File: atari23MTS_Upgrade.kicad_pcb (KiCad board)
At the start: 2 copper layers, 164.5 x 93 mm, 83 parts, among them J1 Micro_SD_Card_Det, P1 CONN_01X01, P2 CONN_01X01, P3 CONN_01X01, P4 CONN_01X01, P5 CONN_01X01, P6 CONN_01X01, SW1 SW_PUSH, U1 NCP1117ST33T3G, U10 ISSI61WV5128BL, U11 ISSI61WV5128BL, U12 ISSI61WV5128BL, U13 ISSI61WV5128BL, U14 74LS08, U15 74LS08, U16 74LS08, U17 STM32F407VETx, U2 74LS138, U3 74HC04, U4 TXB0108-PW, U5 TXB0108-PW, U6 TXB0108-PW, U7 74HC04, U8 TXB0108-PW, U9 TXB0108-PW

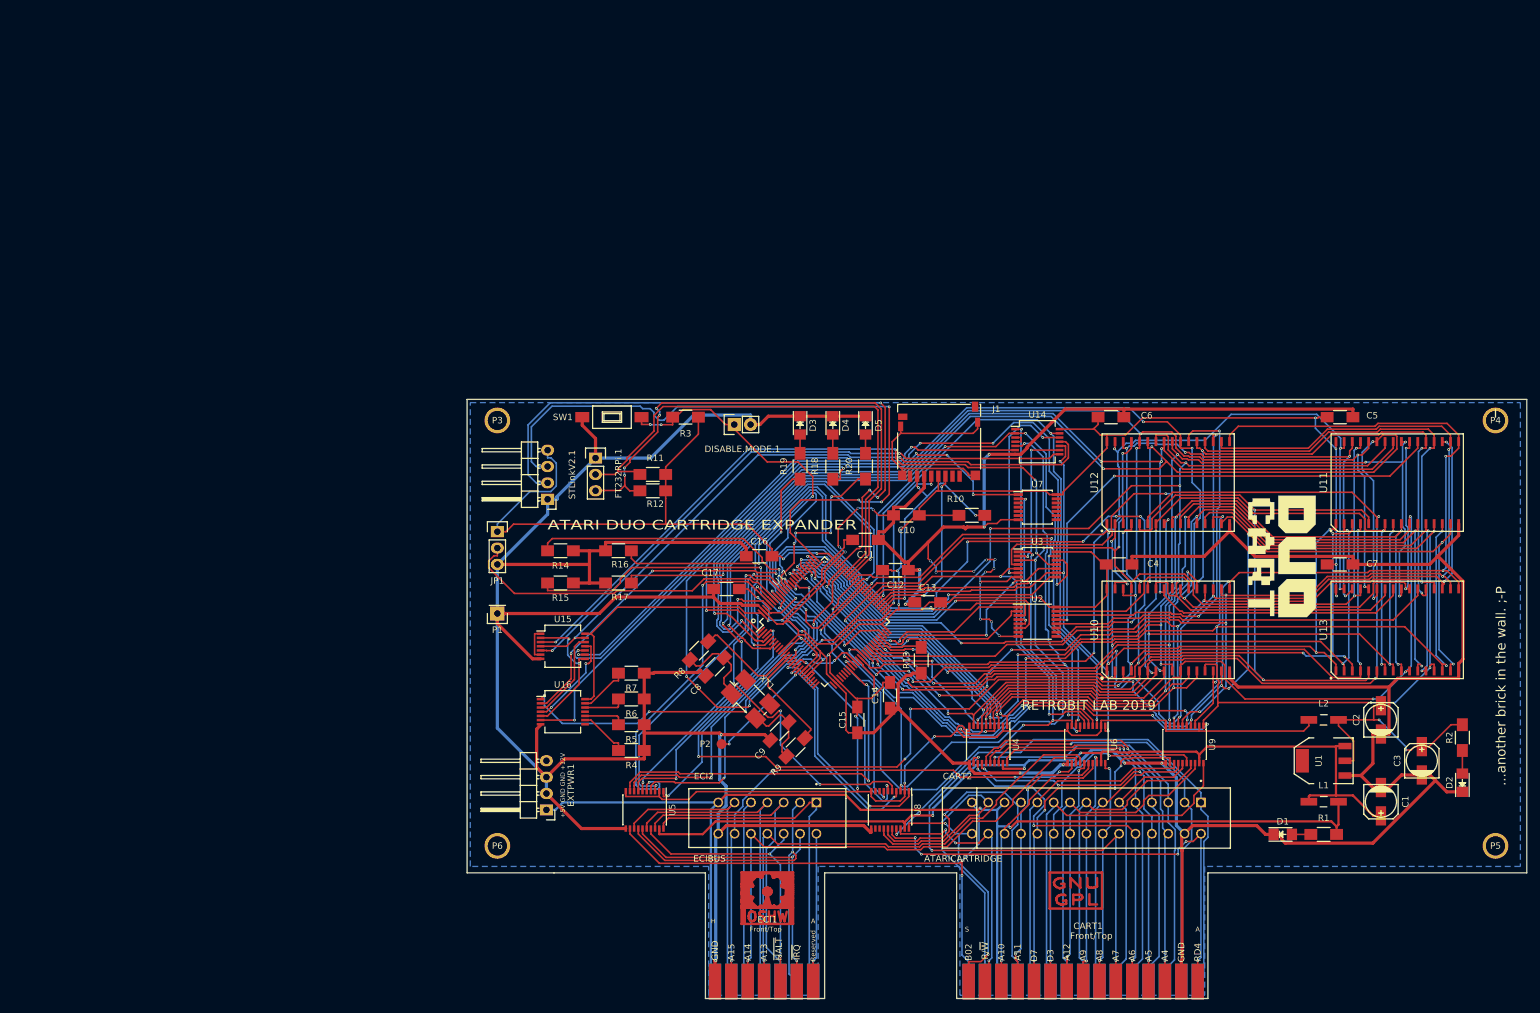
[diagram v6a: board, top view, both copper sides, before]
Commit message: Upgraded with the latest infos
Now there is no logic for address/decoding. All is done inside the
microprocessor. This is a semi-final release.
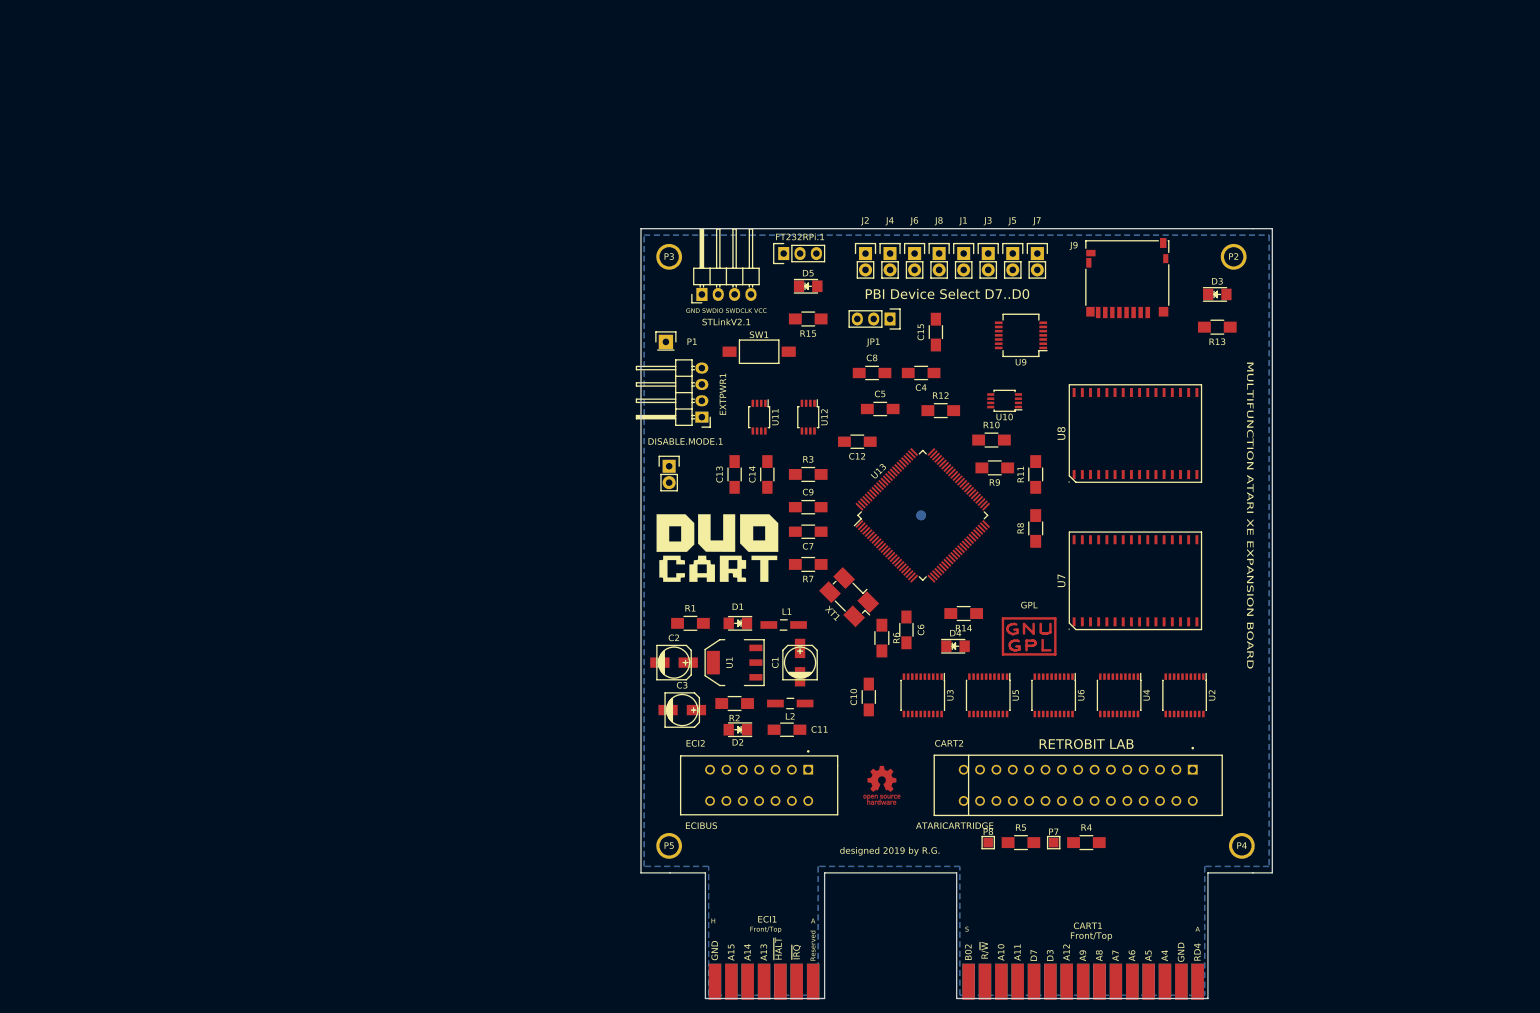
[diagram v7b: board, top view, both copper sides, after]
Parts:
- removed ATARI LOGO FUJI: LOGO, RetroBitLab:atari_fuji_SilkScreen_21.2x25-RevBack
- removed C16, C17: 100n, Capacitors_SMD:C_1206_HandSoldering
- removed R16, R17: 0, Resistors_SMD:R_1206_HandSoldering
- removed R18, R19, R20: 220, Resistors_SMD:R_1206_HandSoldering
- removed REF**: Symbol_GNU-GPL_CopperTop_Small, Symbol:Symbol_GNU-GPL_CopperTop_Small
- removed REF**: Symbol_OSHW-Logo_CopperTop_Negative, Symbols:Symbol_OSHW-Logo_CopperTop_Negative
- removed U14, U15, U16: 74LS08, Housings_SSOP:SSOP-14_5.3x6.2mm_Pitch0.65mm
- removed U17: STM32F407VETx, Housings_QFP:LQFP-100_14x14mm_Pitch0.5mm
- added ATARILOGO: LOGO, RetroBitLab:atari_fuji_SilkScreen_21.2x25-RevBack, B.Cu at (142.2, 49.5)
- added G***: LOGO, RetroBitLab:atari_800_XL_BW_25x25, B.Cu at (144.8, 74.9)
- added GPL: Symbol_GNU-GPL_CopperTop_Small, Symbol:Symbol_GNU-GPL_CopperTop_Small, F.Cu at (158.8, 82.5)
- added J2: Conn_01x02, Pin_Headers:Pin_Header_Straight_1x02, F.Cu at (133.3, 22.9)
- added J3: Conn_01x02, Pin_Headers:Pin_Header_Straight_1x02, F.Cu at (152.4, 22.9)
- added J4: Conn_01x02, Pin_Headers:Pin_Header_Straight_1x02, F.Cu at (137.2, 22.9)
- added J5: Conn_01x02, Pin_Headers:Pin_Header_Straight_1x02, F.Cu at (156.2, 22.9)
- added J6: Conn_01x02, Pin_Headers:Pin_Header_Straight_1x02, F.Cu at (141.0, 22.9)
- added J7: Conn_01x02, Pin_Headers:Pin_Header_Straight_1x02, F.Cu at (160.0, 22.9)
- added J8: Conn_01x02, Pin_Headers:Pin_Header_Straight_1x02, F.Cu at (144.8, 22.9)
- added J9: Micro_SD_Card_Det, RetroBitLab:microSD_HC_Hirose_DM3D-SF, F.Cu at (174.0, 26.7)
- added OSHW: OSHW-Logo_5.7x6mm_Copper, Symbol:OSHW-Logo_5.7x6mm_Copper, F.Cu at (135.9, 105.4)
- added P7: CONN_01X01, TestPoint:TestPoint_Pad_1.5x1.5mm, F.Cu at (162.6, 114.3)
- added P8: CONN_01X01, TestPoint:TestPoint_Pad_1.5x1.5mm, F.Cu at (152.4, 114.3)
- C6, C7: value 100n -> 20p
- C8, C9: value 20p -> 100n
- J1: value Micro_SD_Card_Det -> Conn_01x02; footprint RetroBitLab:microSD_HC_Hirose_DM3D-SF -> Pin_Headers:Pin_Header_Straight_1x02
- P2: footprint Measurement_Points:Measurement_Point_Round-SMD-Pad_Small -> RetroBitLab:MountingHole
- P6: footprint RetroBitLab:MountingHole -> Measurement_Points:Measurement_Point_Round-SMD-Pad_Small; moved to B.Cu
- R10: value 47k -> 10k
- R11, R12: value 10k -> 10K
- R13, R14, R15, R7: value 0 -> 220
- R8: value 0 -> 47k
- R9: value 220 -> 10k
- SW1: value SW_PUSH -> SW_Push; footprint Buttons_Switches_SMD:SW_SPST_FSMSM -> RetroBitLab:SW_SPST_FSMSM_3D
- U10: value ISSI61WV5128BL -> 74LVC2G32; footprint RetroBitLab:SOP-32L-20.5x11.30-1.27mm -> Housings_SSOP:TSSOP-8_3x3mm_Pitch0.65mm
- U11: value ISSI61WV5128BL -> 74LVC2G08; footprint RetroBitLab:SOP-32L-20.5x11.30-1.27mm -> Housings_SSOP:TSSOP-8_3x3mm_Pitch0.65mm
- U12: value ISSI61WV5128BL -> 74LVC2G74; footprint RetroBitLab:SOP-32L-20.5x11.30-1.27mm -> Housings_SSOP:TSSOP-8_3x3mm_Pitch0.65mm
- U13: value ISSI61WV5128BL -> STM32F407VETx; footprint RetroBitLab:SOP-32L-20.5x11.30-1.27mm -> Housings_QFP:LQFP-100_14x14mm_Pitch0.5mm
- U2: value 74LS138 -> TXB0108-PW; footprint Housings_SSOP:TSSOP-16_4.4x5mm_Pitch0.65mm -> Housings_SSOP:SSOP-20_4.4x6.5mm_Pitch0.65mm
- U3: value 74HC04 -> TXB0108-PW; footprint Housings_SSOP:TSSOP-14_4.4x5mm_Pitch0.65mm -> Housings_SSOP:SSOP-20_4.4x6.5mm_Pitch0.65mm
- U7: value 74HC04 -> ISSI61WV5128BL; footprint Housings_SSOP:TSSOP-14_4.4x5mm_Pitch0.65mm -> RetroBitLab:SOP-32L-20.5x11.30-1.27mm
- U8: value TXB0108-PW -> ISSI61WV5128BL; footprint Housings_SSOP:SSOP-20_4.4x6.5mm_Pitch0.65mm -> RetroBitLab:SOP-32L-20.5x11.30-1.27mm
- U9: value TXB0108-PW -> 74HCT04; footprint Housings_SSOP:SSOP-20_4.4x6.5mm_Pitch0.65mm -> Housings_SSOP:SSOP-14_5.3x6.2mm_Pitch0.65mm
- moved P5 128.3 mm to (102.9, 114.3)
- moved C3 115.1 mm to (104.9, 93.7), turned to 0 degrees
- moved R2 113.1 mm to (113.0, 92.7), turned to 180 degrees
- moved D2 112.8 mm to (113.5, 96.8), turned to 180 degrees
- moved C2 110.1 mm to (103.6, 86.4), turned to 0 degrees
- moved P2 110.1 mm to (190.5, 22.9)
- moved R1 103.6 mm to (106.2, 80.3), turned to 0 degrees
- moved U11 99.6 mm to (116.8, 48.3), turned to 270 degrees
- moved C1 92.7 mm to (123.2, 86.4), turned to 90 degrees
- moved U1 92.7 mm to (113.0, 86.4)
- moved D1 90.7 mm to (113.5, 80.3), turned to 180 degrees
- moved L1 88.2 mm to (120.7, 80.5), turned to 180 degrees
- moved DUOCART 87.5 mm to (110.5, 68.6), turned to 0 degrees
- moved P6 83.1 mm to (142.0, 63.5)
- moved L2 82.8 mm to (121.7, 92.7), turned to 180 degrees
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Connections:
- C10 pad 1: VCC3V3 -> GND
- C10 pad 2: GND -> VCC3V3
- C6 pad 1: VCC3V3 -> Net-(C6-Pad1)
- C7 pad 1: VCC3V3 -> Net-(C7-Pad1)
- C8 pad 1: Net-(C8-Pad1) -> VCC3V3
- C9 pad 1: Net-(C9-Pad1) -> GND
- C9 pad 2: GND -> VCC3V3
- J1 pad 1: (no net) -> PBIDEV
- J1 pad 2: (no net) -> mD3
- P2 pad 1: TP1 -> (no net)
- P6 pad 1: (no net) -> TP1
- R10 pad 2: mSDO -> UART_TX_TTL
- R11 pad 2: UART_RX_TTL -> ~mCHIP0
- R12 pad 2: UART_TX_TTL -> ~mCHIP1
- R13 pad 1: GND -> Net-(D3-Pad2)
- R13 pad 2: /MCU/SPARE1 -> LEDGRN
- R14 pad 1: GND -> Net-(D4-Pad2)
- R14 pad 2: /MCU/SPARE2 -> LEDRED
- R15 pad 1: GND -> Net-(D5-Pad2)
- R15 pad 2: /MCU/SPARE3 -> LEDAMBER
- R4 pad 1: GND -> Net-(P7-Pad1)
- R4 pad 2: Net-(R4-Pad2) -> SPARE1
- R5 pad 1: GND -> Net-(P8-Pad1)
- R5 pad 2: Net-(R5-Pad2) -> SPARE2
- R6 pad 1: GND -> Net-(R6-Pad1)
- R6 pad 2: Net-(R6-Pad2) -> Net-(C6-Pad1)
- R7 pad 1: GND -> Net-(R7-Pad1)
- R7 pad 2: Net-(R7-Pad2) -> Net-(C7-Pad1)
- R8 pad 1: Net-(R8-Pad1) -> VCC3V3
- R8 pad 2: Net-(C8-Pad1) -> mSDO
- R9 pad 1: Net-(R9-Pad1) -> VCC3V3
- R9 pad 2: Net-(C9-Pad1) -> UART_RX_TTL
- U10 pad 1: mD1E2_A17 -> ~mD8XX-DFXX
- U10 pad 2: mD1E2_A16 -> Net-(U10-Pad2)
- U10 pad 3: mD1E0_A14 -> (no net)
- U10 pad 4: mD1E0_A12 -> GND
- U10 pad 5: mA7 -> (no net)
- U10 pad 6: mA6 -> (no net)
- U10 pad 7: mA5 -> ~mMPD
- U10 pad 8: mA4 -> +5VDC
- U11 pad 1: mD1E2_A17 -> mPBISEL
- U11 pad 2: mD1E2_A16 -> PBIDEV
- U11 pad 3: mD1E0_A14 -> Net-(U11-Pad3)
- U11 pad 4: mD1E0_A12 -> GND
- U11 pad 5: mA7 -> mW/~R
- U11 pad 6: mA6 -> mPBISEL
- U11 pad 7: mA5 -> Net-(U11-Pad7)
- U11 pad 8: mA4 -> +5VDC
- U12 pad 1: mD1E2_A17 -> Net-(U11-Pad3)
- U12 pad 2: mD1E2_A16 -> Net-(U11-Pad7)
- U12 pad 3: mD1E0_A14 -> Net-(U10-Pad2)
- U12 pad 4: mD1E0_A12 -> GND
- U12 pad 5: mA7 -> (no net)
- U12 pad 6: mA6 -> nRESET
- U12 pad 7: mA5 -> nRESET
- U12 pad 8: mA4 -> +5VDC
- U13 pad 1: mD1E2_A17 -> (no net)
- U13 pad 10: mA2 -> GND
- U13 pad 11: mA1 -> VCC3V3
- U13 pad 12: mA0 -> Net-(R6-Pad1)
- U13 pad 13: mD0 -> Net-(R7-Pad1)
- U13 pad 14: mD1 -> nRESET
- U13 pad 15: mD2 -> mB02/PHI2
- U13 pad 16: GND -> ~mS5
- U13 pad 17: mD3 -> ~mS4
- U13 pad 18: mD4 -> TP1
- U13 pad 19: mD5 -> VCC3V3
- U13 pad 2: mD1E2_A16 -> (no net)
- U13 pad 20: mD6 -> GND
- U13 pad 21: mD7 -> VCC3V3
- U13 pad 22: ~BSEL3 -> VCC3V3
- U13 pad 23: mD1E0_A10 -> (no net)
- U13 pad 24: ~mOE -> (no net)
- U13 pad 25: mD1E0_A11 -> (no net)
- U13 pad 26: mD1E0_A9 -> (no net)
- U13 pad 27: mD1E0_A8 -> GND
- U13 pad 28: mD1E0_A13 -> VCC3V3
- U13 pad 29: mR/~W -> (no net)
- U13 pad 3: mD1E0_A14 -> (no net)
- U13 pad 30: mD1E2_A18 -> (no net)
- U13 pad 31: mD1E0_A15 -> (no net)
- U13 pad 32: VCC3V3 -> (no net)
- U13 pad 4: mD1E0_A12 -> (no net)
- U13 pad 5: mA7 -> (no net)
- U13 pad 6: mA6 -> (no net)
- U13 pad 7: mA5 -> mPBISEL
- U13 pad 8: mA4 -> mSPARE1
- U13 pad 9: mA3 -> mSPARE2
- U2 pad 1: mD1E2_A19 -> mA0
- U2 pad 10: (no net) -> VCC3V3
- U2 pad 11: (no net) -> GND
- U2 pad 12: ~BSEL3 -> A7
- U2 pad 13: ~BSEL2 -> A6
- U2 pad 14: ~BSEL1 -> A5
- U2 pad 15: ~BSEL0 -> A4
- U2 pad 16: VCC3V3 -> A3
- U2 pad 2: mD1E3_A20 -> VCC3V3
- U2 pad 3: mD1E3_A21 -> mA1
- U2 pad 4: ~mD6XX -> mA2
- U2 pad 5: ~mD6XX -> mA3
- U2 pad 6: RAMEN -> mA4
- U2 pad 7: (no net) -> mA5
- U2 pad 8: GND -> mA6
- U2 pad 9: (no net) -> mA7
- U3 pad 1: mA10 -> ~mEXSEL
- U3 pad 10: ~mD3XX -> VCC3V3
- U3 pad 11: mD3XX -> GND
- U3 pad 12: ~mA13 -> ~CCTL
- U3 pad 13: mA13 -> ~REF
- U3 pad 14: VCC3V3 -> ~RST
- U3 pad 2: ~mA10 -> VCC3V3
- U3 pad 3: mR/~W -> ~mD1XX
- U3 pad 4: ~mOE -> ~mHALT
- U3 pad 5: mA11 -> ~mMPD
- U3 pad 6: ~mA11 -> ~mIRQ
- U3 pad 7: GND -> ~mRST
- U3 pad 8: ~mA8 -> ~mREF
- U3 pad 9: mA8 -> ~mCCTL
- U4 pad 1: mA0 -> mA8
- U4 pad 12: A7 -> A15
- U4 pad 13: A6 -> A14
- U4 pad 14: A5 -> A13
- U4 pad 15: A4 -> A12
- U4 pad 16: A3 -> A11
- U4 pad 17: A2 -> A10
- U4 pad 18: A1 -> A9
- U4 pad 20: A0 -> A8
- U4 pad 3: mA1 -> mA9
- U4 pad 4: mA2 -> mA10
- U4 pad 5: mA3 -> mA11
- U4 pad 6: mA4 -> mA12
- U4 pad 7: mA5 -> mA13
- U4 pad 8: mA6 -> mA14
- U4 pad 9: mA7 -> mA15
- U5 pad 1: ~mEXSEL -> mB02/PHI2
- U5 pad 12: ~CCTL -> SPARE2
- U5 pad 13: ~REF -> SPARE1
- U5 pad 14: ~RST -> RD5
- U5 pad 15: ~IRQ -> ~S5
- U5 pad 16: ~MPD -> RD4
- U5 pad 17: ~HALT -> ~S4
- U5 pad 18: ~D1XX -> R/~W
- U5 pad 20: ~EXSEL -> B02/PHI2
- U5 pad 3: ~mD1XX -> mR/~W
- U5 pad 4: ~mHALT -> ~mS4
- U5 pad 5: ~mMPD -> mRD4
- U5 pad 6: ~mIRQ -> ~mS5
- U5 pad 7: ~mRST -> mRD5
- U5 pad 8: ~mREF -> mSPARE1
- U5 pad 9: ~mCCTL -> mSPARE2
- U6 pad 1: mA8 -> mD0
- U6 pad 12: A15 -> D7
- U6 pad 13: A14 -> D6
- U6 pad 14: A13 -> D5
- U6 pad 15: A12 -> D4
- U6 pad 16: A11 -> D3
- U6 pad 17: A10 -> D2
- U6 pad 18: A9 -> D1
- U6 pad 20: A8 -> D0
- U6 pad 3: mA9 -> mD1
- U6 pad 4: mA10 -> mD2
- U6 pad 5: mA11 -> mD3
- U6 pad 6: mA12 -> mD4
- U6 pad 7: mA13 -> mD5
- U6 pad 8: mA14 -> mD6
- U6 pad 9: mA15 -> mD7
- U7 pad 1: mD6XX -> mxA17
- U7 pad 10: (no net) -> mA2
- U7 pad 11: (no net) -> mA1
- U7 pad 12: (no net) -> mA0
- U7 pad 13: (no net) -> mD0
- U7 pad 14: VCC3V3 -> mD1
- U7 pad 2: ~mD6XX -> mxA16
- U7 pad 3: (no net) -> mxA14
- U7 pad 4: (no net) -> mA12
- U7 pad 5: (no net) -> mA7
- U7 pad 6: (no net) -> mA6
- U7 pad 7: GND -> mA5
- U7 pad 8: (no net) -> mA4
- U7 pad 9: (no net) -> mA3
- U8 pad 1: mB02/PHI2 -> mxA17
- U8 pad 10: VCC3V3 -> mA2
- U8 pad 11: GND -> mA1
- U8 pad 12: (no net) -> mA0
- U8 pad 13: (no net) -> mD0
- U8 pad 14: RD5 -> mD1
- U8 pad 15: ~S5 -> mD2
- U8 pad 16: RD4 -> GND
- U8 pad 17: ~S4 -> mD3
- U8 pad 18: R/~W -> mD4
- U8 pad 19: VCC5V -> mD5
- U8 pad 2: VCC3V3 -> mxA16
- U8 pad 20: B02/PHI2 -> mD6
- U8 pad 3: mR/~W -> mxA14
- U8 pad 4: ~mS4 -> mA12
- U8 pad 5: mRD4 -> mA7
- U8 pad 6: ~mS5 -> mA6
- U8 pad 7: mRD5 -> mA5
- U8 pad 8: (no net) -> mA4
- U8 pad 9: (no net) -> mA3
- U9 pad 1: mD0 -> mR/~W
- U9 pad 10: VCC3V3 -> (no net)
- U9 pad 12: D7 -> (no net)
- U9 pad 13: D6 -> GND
- U9 pad 14: D5 -> VCC3V3
- U9 pad 2: VCC3V3 -> mW/~R
- U9 pad 3: mD1 -> GND
- U9 pad 4: mD2 -> (no net)
- U9 pad 5: mD3 -> GND
- U9 pad 6: mD4 -> (no net)
- U9 pad 7: mD5 -> GND
- U9 pad 8: mD6 -> (no net)
- U9 pad 9: mD7 -> GND
- XT1 pad 1: Net-(C8-Pad1) -> Net-(C6-Pad1)
- XT1 pad 2: Net-(C9-Pad1) -> Net-(C7-Pad1)
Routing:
- net GND: track 910.3 -> 0.00 mm, vias 25 -> 0
- net VCC3V3: track 554.3 -> 0.00 mm, vias 20 -> 0
- net mD1E0_A11: track 205.7 -> 0.00 mm, vias 5 -> 0
- net mD1E0_A8: track 203.9 -> 0.00 mm, vias 6 -> 0
- net mD1E0_A9: track 196.5 -> 0.00 mm, vias 5 -> 0
- net mD1E0_A10: track 195.7 -> 0.00 mm, vias 6 -> 0
- net mD1E0_A12: track 193.5 -> 0.00 mm, vias 9 -> 0
- net mD1E0_A14: track 192.4 -> 0.00 mm, vias 9 -> 0
- net mR/~W: track 188.7 -> 0.00 mm, vias 8 -> 0
- net +5VDC: track 188.0 -> 0.00 mm, vias 2 -> 0
- net mA2: track 187.3 -> 0.00 mm, vias 5 -> 0
- net mD4: track 183.2 -> 0.00 mm, vias 5 -> 0
- net mD1E0_A13: track 183.0 -> 0.00 mm, vias 6 -> 0
- net mD3: track 183.0 -> 0.00 mm, vias 7 -> 0
- net mD0: track 182.4 -> 0.00 mm, vias 7 -> 0
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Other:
- board size 164.5 x 93 mm -> 98 x 119.5 mm
- board text added: "GND SWDIO SWDCLK VCC"
- board text added: "MULTIFUNCTION ATARI XE EXPANSION BOARD"
- board text added: "PBI Device Select D7..D0"
- board text added: "RETROBIT LAB"
- board text added: "designed 2019 by R.G."
- board text removed: "+5V GND GND +12V"
- board text removed: "...another brick in the wall. ;-P"
- board text removed: "8-BIT"
- board text removed: "ATARI DUO CARTRIDGE EXPANDER"
- board text removed: "RETROBIT LAB 2019"
- board text removed: "designed by R.G.2019"

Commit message: Upgraded after last routing
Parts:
- removed GPL: Symbol_GNU-GPL_CopperTop_Small, Symbol:Symbol_GNU-GPL_CopperTop_Small
- added Kicad: KiCad-Logo_5mm_SilkScreen, Symbol:KiCad-Logo_5mm_SilkScreen, F.Cu at (155.0, 74.0)
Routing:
- net GND: track 0.00 -> 629.3 mm, vias 0 -> 11
- net VCC3V3: track 0.00 -> 429.5 mm, vias 0 -> 10
- net +5VDC: track 0.00 -> 243.0 mm, vias 0 -> 4
- net mD7: track 0.00 -> 142.6 mm, vias 0 -> 2
- net mD2: track 0.00 -> 136.9 mm, vias 0 -> 3
- net mD6: track 0.00 -> 134.9 mm, vias 0 -> 4
- net mD5: track 0.00 -> 134.8 mm, vias 0 -> 3
- net mD3: track 0.00 -> 134.2 mm, vias 0 -> 3
- net mD4: track 0.00 -> 127.9 mm, vias 0 -> 4
- net mD0: track 0.00 -> 124.7 mm, vias 0 -> 6
- net mD1: track 0.00 -> 122.5 mm, vias 0 -> 5
- net A15: track 0.00 -> 103.5 mm, vias 0 -> 1
- net mW/~R: track 0.00 -> 103.1 mm, vias 0 -> 4
- net mR/~W: track 0.00 -> 96.3 mm, vias 0 -> 6
- net A14: track 0.00 -> 92.8 mm, vias 0 -> 1
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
